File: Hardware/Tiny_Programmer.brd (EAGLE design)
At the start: 59.7 x 15.2 mm, 31 parts, among them Q1 16MHz, U1 ATTINY84, X1 USB-A-H

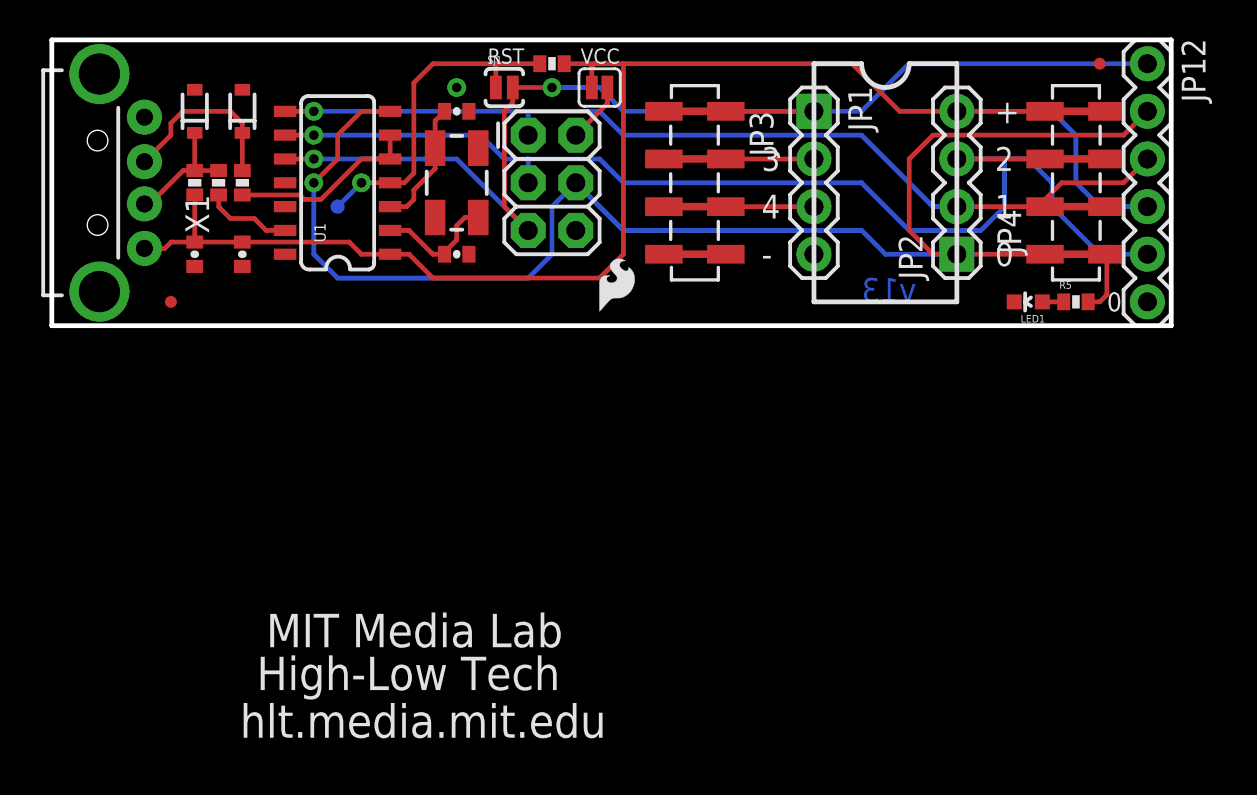
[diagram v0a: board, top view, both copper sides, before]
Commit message: replace USB port, and redraw board
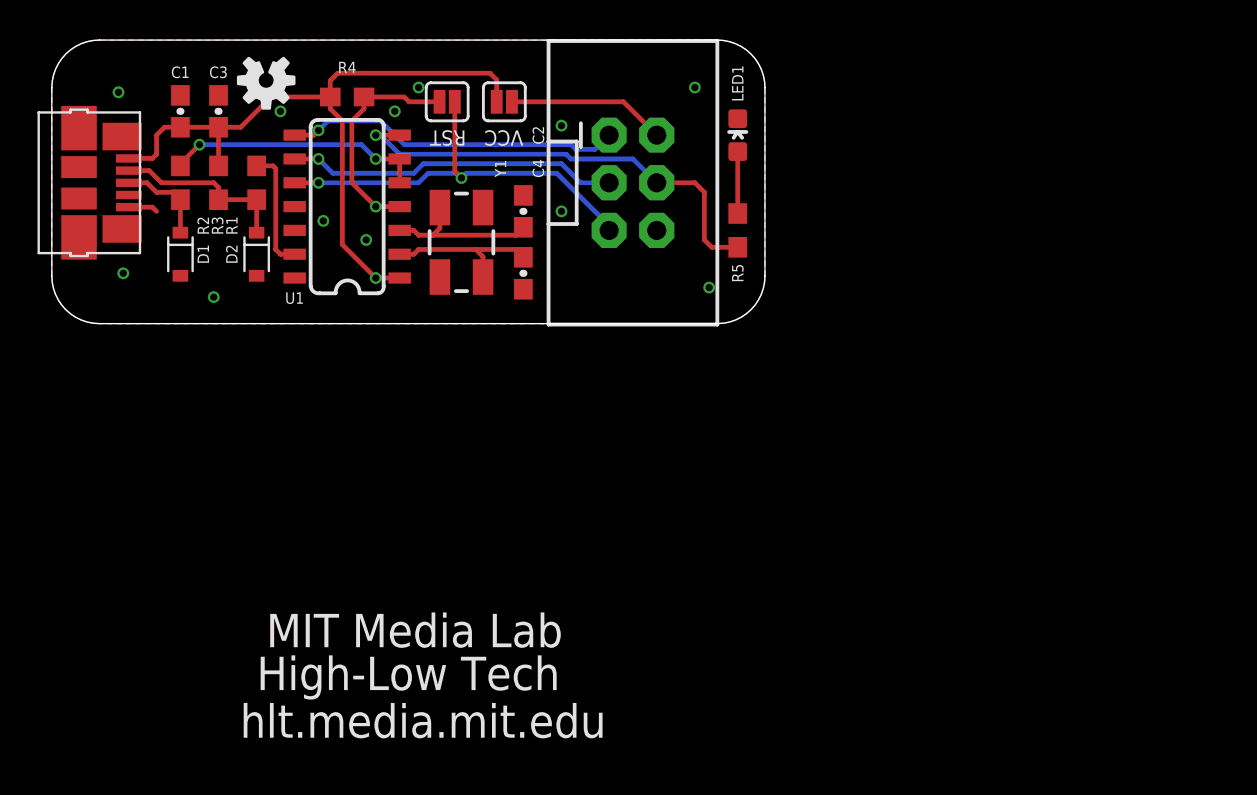
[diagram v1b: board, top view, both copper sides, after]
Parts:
- removed JP11, JP6: LOGO-SFESK, SparkFun-Aesthetics:SFE-LOGO-FLAME
- removed JP12: (no value), SparkFun-Connectors:1X06
- removed JP2: (no value), SparkFun-Connectors:1X04
- removed JP3, JP4: (no value), SparkFun-Connectors:1X04_SMD_STRAIGHT_COMBO
- removed JP5: LOGO-SFENW2, SparkFun-Aesthetics:SFE-NEW-WEB
- removed JP7, JP8: FIDUCIALUFIDUCIAL, SparkFun:MICRO-FIDUCIAL
- removed JP9: (no value), SparkFun-Connectors:2X3
- removed Q1: 16MHz, SparkFun-FreqCtrl:CRYSTAL-SMD-5X3
- removed TP1: TEST-POINT3, SparkFun-Passives:PAD.03X.03
- removed X1: USB-A-H, SparkFun-Connectors:USB-A-H
- added CN1: USBMICROB-MOLEX-47346-0001, Connectors:MOLEX_47346-0001
- added Y1: 16MHz, SparkFun-Clocks:CRYSTAL-SMD-5X3.2-4PAD
- C1, C2, C3, C4: device SparkFun-Passives:0402-CAP -> Darryl-Capacitors:0603-CAP
- D1, D2: value 3.3V -> 3V3; device SparkFun-DiscreteSemi:SOD-323 -> Darryl-DiscreteSemi:SOD-323
- JP1: value (none) -> M03X2-SHROUDED; device SparkFun-Connectors:1X04 -> Darryl:2X3-SHROUDED-B
- LED1: value Yellow -> (none); device SparkFun-LED:LED-0603 -> Darryl:LED-0603
- R1, R2: value 68 -> 68R; device SparkFun-Passives:0402-RES -> Darryl-Resistors:0603-RES
- R3: value 1.5K -> 1K5; device SparkFun-Passives:0402-RES -> Darryl-Resistors:0603-RES
- R4: value 10k -> 10K; device SparkFun-Passives:0402-RES -> Darryl-Resistors:0603-RES
- R5: value 330 -> 330R; device SparkFun-Passives:0402-RES -> Darryl-Resistors:0603-RES
- SJ1: value SOLDERJUMPERNO -> JUMPER-SMT_2_NO_SILK; device SparkFun-Passives:SJ_2S-NO -> SparkFun-Jumpers:SMT-JUMPER_2_NO_SILK
- SJ2: value NC -> JUMPER-SMT_2_NO_SILK; device SparkFun-Passives:SJ_2S -> SparkFun-Jumpers:SMT-JUMPER_2_NO_SILK
- moved U$1 33.4 mm to (11.4, 13.1), flipped to the top, turned to 180 degrees
- moved R5 18.4 mm to (36.6, 5.08), turned to 270 degrees
- moved LED1 17.9 mm to (36.6, 10.2), turned to 0 degrees
- moved R4 11.1 mm to (15.7, 12.2), turned to 180 degrees
- moved JP1 10.4 mm to (31.0, 7.62)
- moved D1 8.30 mm to (6.86, 3.81), turned to 270 degrees
- moved D2 8.30 mm to (10.9, 3.81), turned to 270 degrees
- moved C3 7.73 mm to (8.89, 11.4), turned to 90 degrees
- moved C1 7.66 mm to (6.86, 11.4), turned to 90 degrees
- moved C2 6.41 mm to (25.1, 6.10), turned to 90 degrees
- moved SJ2 5.14 mm to (24.1, 11.9)
- moved C4 3.70 mm to (25.1, 2.79), turned to 270 degrees
- moved R2 3.30 mm to (6.86, 7.62), turned to 90 degrees
- moved SJ1 3.14 mm to (21.1, 11.9), turned to 180 degrees
- moved R1 2.03 mm to (10.9, 7.62), turned to 90 degrees
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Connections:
- removed net 2: JP1.2, JP3.2
- removed net 3: JP1.3, JP3.3
- removed net VCC: C1.1, C3.1, JP12.4, JP2.4, JP4.4, R3.2, R4.2, SJ2.1, U1.1, X1.VBUS
- new net V_USB: C1.1, C3.1, CN1.1, R3.2, R4.2, SJ2.1, U1.1
- net GND: now also CN1.5, CN1.SHIELD1, CN1.SHIELD2, CN1.SHIELD3, CN1.SHIELD4, CN1.SHIELD5, CN1.SHIELD6, D1.A, D2.A, JP1.6; no longer D1.2, D2.2, JP1.4, JP12.6, JP3.4, JP9.6, X1.GND
- net MISO: now also JP1.1; no longer JP12.3, JP2.2, JP4.2, JP9.1
- net MOSI: now also JP1.4; no longer JP12.2, JP2.1, JP4.1, JP9.4
- net N$1: now also CN1.2, D2.C; no longer D2.1, X1.D-
- net N$2: now also CN1.3, D1.C; no longer D1.1, X1.D+
- net N$3: now also Y1.1; no longer Q1.3
- net N$4: now also Y1.3; no longer Q1.1
- net RESET: now also SJ1.2; no longer SJ1.1, TP1.P$1
- net RST: now also JP1.5, SJ1.1; no longer JP1.1, JP12.1, JP3.1, JP9.5, SJ1.2
- net SCK: now also JP1.3; no longer JP12.5, JP2.3, JP4.3, JP9.3
- net VCC': now also JP1.2; no longer JP9.2
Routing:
- net VCC: track 81.5 -> 0.00 mm
- net MOSI: track 82.5 -> 24.5 mm
- net SCK: track 65.8 -> 17.7 mm
- net RST: track 66.3 -> 22.8 mm
- net V_USB: track 0.00 -> 37.9 mm, vias 0 -> 1
- net MISO: track 50.6 -> 18.0 mm
- net 3: track 8.00 -> 0.00 mm
- net RESET: track 18.1 -> 12.0 mm
- net VCC': track 3.24 -> 8.46 mm
- net 2: track 4.70 -> 0.00 mm
- net N$2: track 9.49 -> 4.88 mm
- net D+: track 10.1 -> 13.8 mm, vias 0 -> 2
- net N$1: track 6.70 -> 9.59 mm
- net N$5: track 1.14 -> 3.30 mm
- net N$4: track 6.55 -> 8.51 mm
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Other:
- board size 59.7 x 15.2 mm -> 38 x 15.1 mm
- board text added: "Tinier Programmer v1.0.0"
- board text removed: "+"
- board text removed: "-"
- board text removed: "0"
- board text removed: "1"
- board text removed: "2"
- board text removed: "3"
- board text removed: "4"
- board text removed: "GND"
- board text removed: "ISP"
- board text removed: "Tiny Programmer"
- board text removed: "v13"
